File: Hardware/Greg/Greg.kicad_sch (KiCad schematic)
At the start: 38 parts, among them IC1 TPS61089RNRR, IC2 AP2205-W5-7, J1 1053131104, J3 Conn_01x08_Pin

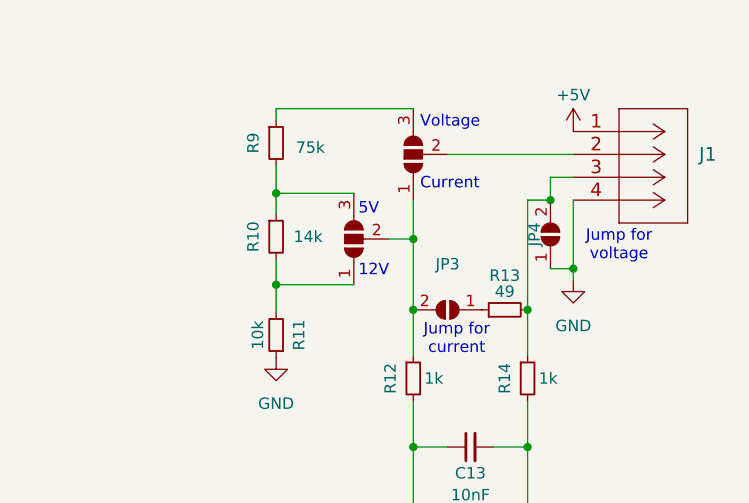
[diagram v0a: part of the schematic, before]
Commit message: updated resistor values for 1.1v ref
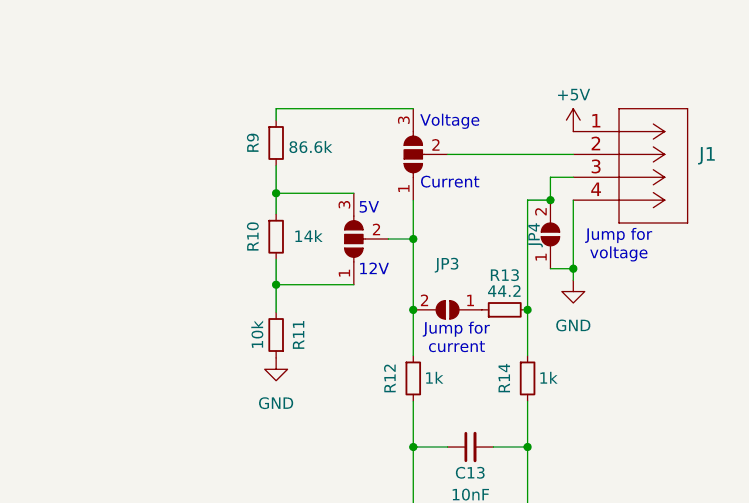
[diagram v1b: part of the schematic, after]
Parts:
- R13: value 49 -> 44.2
- R9: value 75k -> 86.6k
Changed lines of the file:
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@@
 			)
 		)
-		(property "Value" "49"
+		(property "Value" "44.2"
 			(at 223.012 55.88 90)
 			(effects
@@
 			)
 		)
-		(property "Value" "75k"
+		(property "Value" "86.6k"
 			(at 201.422 39.878 0)
 			(effects

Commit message: changed a cap
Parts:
- C11: footprint Capacitor_SMD:C_0402_1005Metric -> Capacitor_SMD:C_0603_1608Metric; MPN (none) -> TMK107BBJ106MA-T
- C12: MPN (none) -> C1005X5R1E104KT000E
- C4: MPN (none) -> C1005X6S1C105KT000E
- C8: MPN (none) -> GRM155R61C225KE11D
- R10: MPN (none) -> 0402WGF1402TCE
- R11: MPN (none) -> ERA2ARB103X
- R13: MPN (none) -> ARG02FTC44R2
- R7: value 152k -> 150k
- R9: MPN (none) -> 0402WGF8662TCE
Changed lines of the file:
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@@
 	)
 	(junction
+		(at 62.992 127.508)
+		(diameter 0)
+		(color 0 0 0 0)
+	)
+	(junction
 		(at 225.552 57.912)
 		(diameter 0)
@@
 	)
 	(junction
-		(at 62.23 127.762)
-		(diameter 0)
-		(color 0 0 0 0)
-	)
-	(junction
 		(at 197.612 55.118)
 		(diameter 0)
@@
 	(wire
 		(pts
-			(xy 62.23 128.016) (xy 62.23 127.762)
-		)
-		(stroke
-			(width 0)
-			(type default)
-		)
-	)
-	(wire
-		(pts
 			(xy 227.838 128.016) (xy 227.838 128.27)
 		)
@@
 	(wire
 		(pts
-			(xy 89.408 104.14) (xy 92.456 104.14)
+			(xy 62.992 127.508) (xy 62.992 127.762)
 		)
 		(stroke
@@
 	(wire
 		(pts
-			(xy 214.884 118.11) (xy 223.012 118.11)
+			(xy 89.408 104.14) (xy 92.456 104.14)
 		)
 		(stroke
@@
 	(wire
 		(pts
-			(xy 212.852 73.152) (xy 216.662 73.152)
+			(xy 214.884 118.11) (xy 223.012 118.11)
 		)
 		(stroke
@@
 	(wire
 		(pts
-			(xy 162.814 148.082) (xy 165.354 148.082)
+			(xy 212.852 73.152) (xy 216.662 73.152)
 		)
 		(stroke
@@
 	(wire
 		(pts
-			(xy 62.23 128.016) (xy 66.04 128.016)
+			(xy 162.814 148.082) (xy 165.354 148.082)
 		)
 		(stroke
@@
 	(wire
 		(pts
-			(xy 66.04 128.016) (xy 66.04 127.508)
-		)
-		(stroke
-			(width 0)
-			(type default)
-		)
-	)
-	(wire
-		(pts
 			(xy 230.632 53.34) (xy 230.632 54.61)
 		)
@@
 	(wire
 		(pts
-			(xy 62.23 127.762) (xy 62.992 127.762)
+			(xy 103.124 40.132) (xy 103.124 37.592)
 		)
 		(stroke
@@
 	(wire
 		(pts
-			(xy 103.124 40.132) (xy 103.124 37.592)
+			(xy 62.992 120.65) (xy 76.708 120.65)
 		)
 		(stroke
@@
 	(wire
 		(pts
-			(xy 62.992 120.65) (xy 76.708 120.65)
+			(xy 214.884 128.27) (xy 227.838 128.27)
 		)
 		(stroke
@@
 	(wire
 		(pts
-			(xy 62.23 125.73) (xy 62.23 127.762)
+			(xy 103.124 37.592) (xy 115.57 37.592)
 		)
 		(stroke
@@
 	(wire
 		(pts
-			(xy 214.884 128.27) (xy 227.838 128.27)
+			(xy 62.992 125.73) (xy 62.992 127.508)
 		)
 		(stroke
@@
 	(wire
 		(pts
-			(xy 103.124 37.592) (xy 115.57 37.592)
+			(xy 62.992 127.508) (xy 65.278 127.508)
 		)
 		(stroke
@@
 	(wire
 		(pts
-			(xy 62.23 125.73) (xy 62.992 125.73)
-		)
-		(stroke
-			(width 0)
-			(type default)
-		)
-	)
-	(wire
-		(pts
 			(xy 61.468 109.22) (xy 61.468 120.65)
 		)
@@
 	)
 	(label "FB_5V"
-		(at 66.04 128.016 0)
+		(at 65.278 127.508 0)
 		(fields_autoplaced yes)
 		(effects
@@
 			)
 		)
+		(property "MPN" "ARG02FTC44R2"
+			(at 223.012 57.912 90)
+			(effects
+				(font
+					(size 1.27 1.27)
+				)
+				(hide yes)
+			)
+		)
 		(pin "1"
 		)
@@
 			)
 		)
+		(property "MPN" "0402WGF1402TCE"
+			(at 197.612 49.784 90)
+			(effects
+				(font
+					(size 1.27 1.27)
+				)
+				(hide yes)
+			)
+		)
 		(pin "1"
 		)
@@
 		(fields_autoplaced yes)
 		(property "Reference" "R7"
-			(at 103.124 34.417 0)
+			(at 102.0826 33.8398 0)
 			(effects
 				(font
@@
 			)
 		)
-		(property "Value" "152k"
-			(at 103.124 36.957 0)
+		(property "Value" "150k"
+			(at 102.0826 36.2641 0)
 			(effects
 				(font
@@
 			)
 		)
-		(property "Footprint" "Capacitor_SMD:C_0402_1005Metric"
+		(property "Footprint" "Capacitor_SMD:C_0603_1608Metric"
 			(at 119.634 66.802 0)
 			(effects
@@
 			)
 		)
+		(property "MPN" " TMK107BBJ106MA-T"
+			(at 119.634 66.802 0)
+			(effects
+				(font
+					(size 1.27 1.27)
+				)
+				(hide yes)
+			)
+		)
 		(pin "1"
 		)
@@
 			)
 		)
+		(property "MPN" " GRM155R61C225KE11D"
+			(at 103.124 42.672 0)
+			(effects
+				(font
+					(size 1.27 1.27)
+				)
+				(hide yes)
+			)
+		)
 		(pin "1"
 		)
@@
 			)
 		)
+		(property "MPN" "ERA2ARB103X"
+			(at 197.612 60.706 90)
+			(effects
+				(font
+					(size 1.27 1.27)
+				)
+				(hide yes)
+			)
+		)
 		(pin "1"
 		)
@@
 			)
 		)
+		(property "MPN" "C1005X5R1E104KT000E"
+			(at 127.254 66.802 0)
+			(effects
+				(font
+					(size 1.27 1.27)
+				)
+				(hide yes)
+			)
+		)
 		(pin "1"
 		)
@@
 			)
 		)
+		(property "MPN" "0402WGF8662TCE"
+			(at 197.612 39.37 90)
+			(effects
+				(font
+					(size 1.27 1.27)
+				)
+				(hide yes)
+			)
+		)
 		(pin "1"
 		)
@@
 			(at 52.324 37.592 0)
 			(effects
+				(font
+					(size 1.27 1.27)
+				)
+				(hide yes)
+			)
+		)
+		(property "MPN" "C1005X6S1C105KT000E"
+			(at 52.324 37.592 0)
+			(effects

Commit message: update
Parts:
- C11: MPN TMK107BBJ106MA-T -> TMK107BBJ106MA-T
- C4: MPN C1005X6S1C105KT000E -> CL05X105KA5NQNC
- C8: MPN GRM155R61C225KE11D -> GRM155R61E225ME15D
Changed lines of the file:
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@@
 			)
 		)
-		(property "MPN" " TMK107BBJ106MA-T"
+		(property "MPN" "TMK107BBJ106MA-T"
 			(at 119.634 66.802 0)
 			(effects
@@
 			)
 		)
-		(property "MPN" " GRM155R61C225KE11D"
+		(property "MPN" " GRM155R61E225ME15D"
 			(at 103.124 42.672 0)
 			(effects
@@
 			)
 		)
-		(property "MPN" "C1005X6S1C105KT000E"
+		(property "MPN" "CL05X105KA5NQNC"
 			(at 52.324 37.592 0)
 			(effects

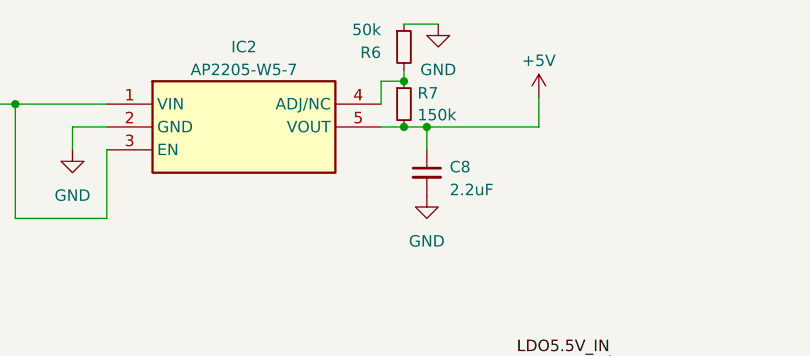
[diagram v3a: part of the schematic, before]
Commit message: changed ldo resistor to match stark
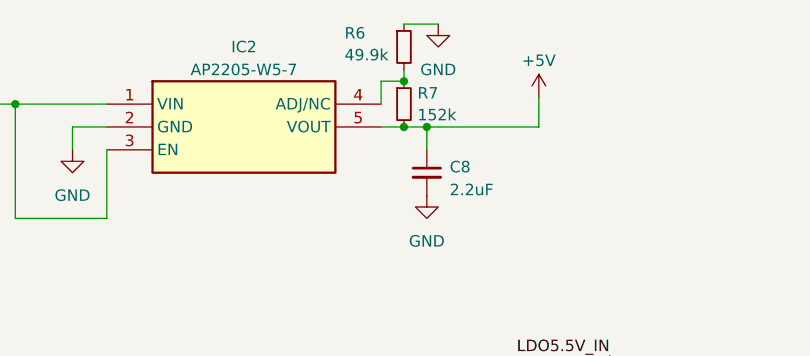
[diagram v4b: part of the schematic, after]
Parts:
- R6: value 50k -> 49.9k
- R7: value 150k -> 152k
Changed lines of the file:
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@@
 		(on_board yes)
 		(dnp no)
-		(fields_autoplaced yes)
 		(property "Reference" "R6"
-			(at 98.044 29.337 0)
-			(effects
-				(font
-					(size 1.27 1.27)
-				)
-				(justify right)
-			)
-		)
-		(property "Value" "50k"
-			(at 98.044 26.797 0)
-			(effects
-				(font
-					(size 1.27 1.27)
-				)
-				(justify right)
+			(at 93.98 27.178 0)
+			(effects
+				(font
+					(size 1.27 1.27)
+				)
+				(justify left)
+			)
+		)
+		(property "Value" "49.9k"
+			(at 93.98 29.6023 0)
+			(effects
+				(font
+					(size 1.27 1.27)
+				)
+				(justify left)
 			)
 		)
@@
 			)
 		)
-		(property "Value" "150k"
+		(property "Value" "152k"
 			(at 102.0826 36.2641 0)
 			(effects

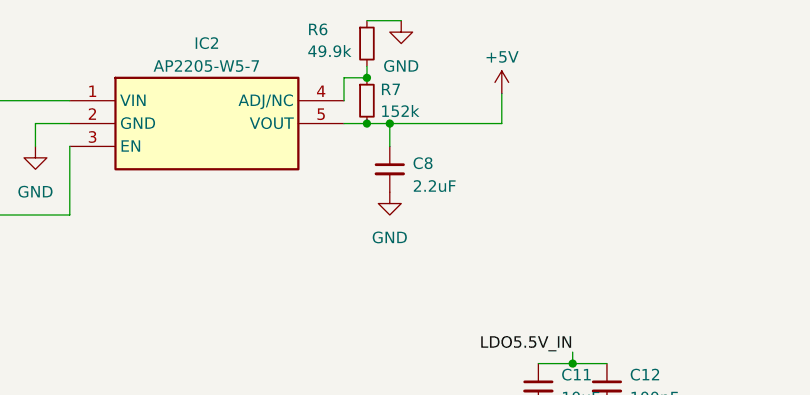
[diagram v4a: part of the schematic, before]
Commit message: changed non standard resistor on ldo
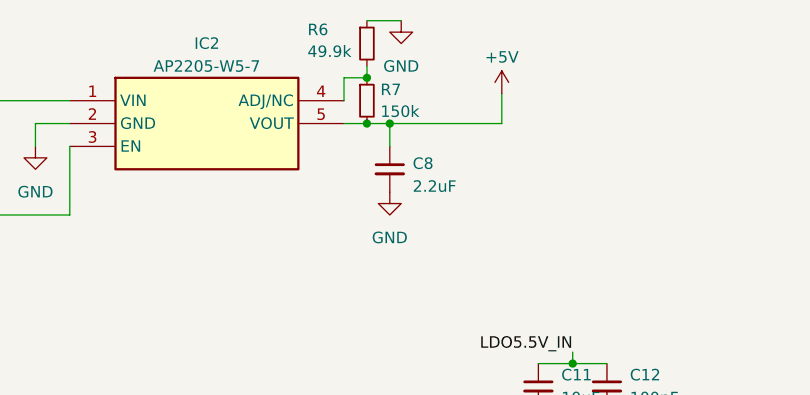
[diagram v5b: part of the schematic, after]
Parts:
- R7: value 152k -> 150k
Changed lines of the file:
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@@
 			)
 		)
-		(property "Value" "152k"
+		(property "Value" "150k"
 			(at 102.0826 36.2641 0)
 			(effects
